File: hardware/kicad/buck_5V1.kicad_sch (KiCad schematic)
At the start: 14 parts, among them J1 12V_IN, J2 12V_IN, Q1 IRF4905

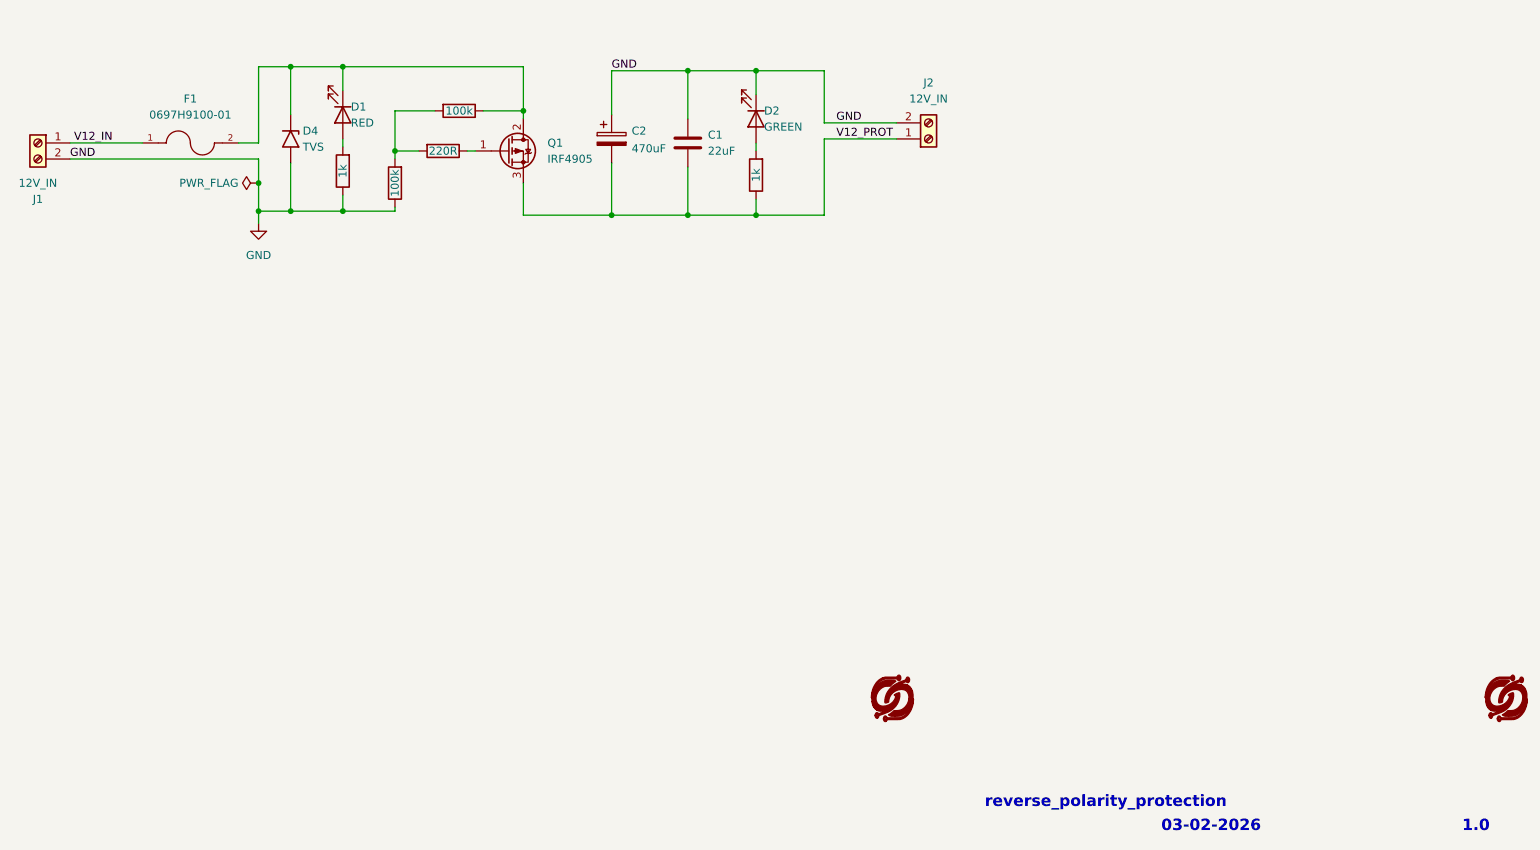
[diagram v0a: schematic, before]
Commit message: feat: added buck_5V1 schematic
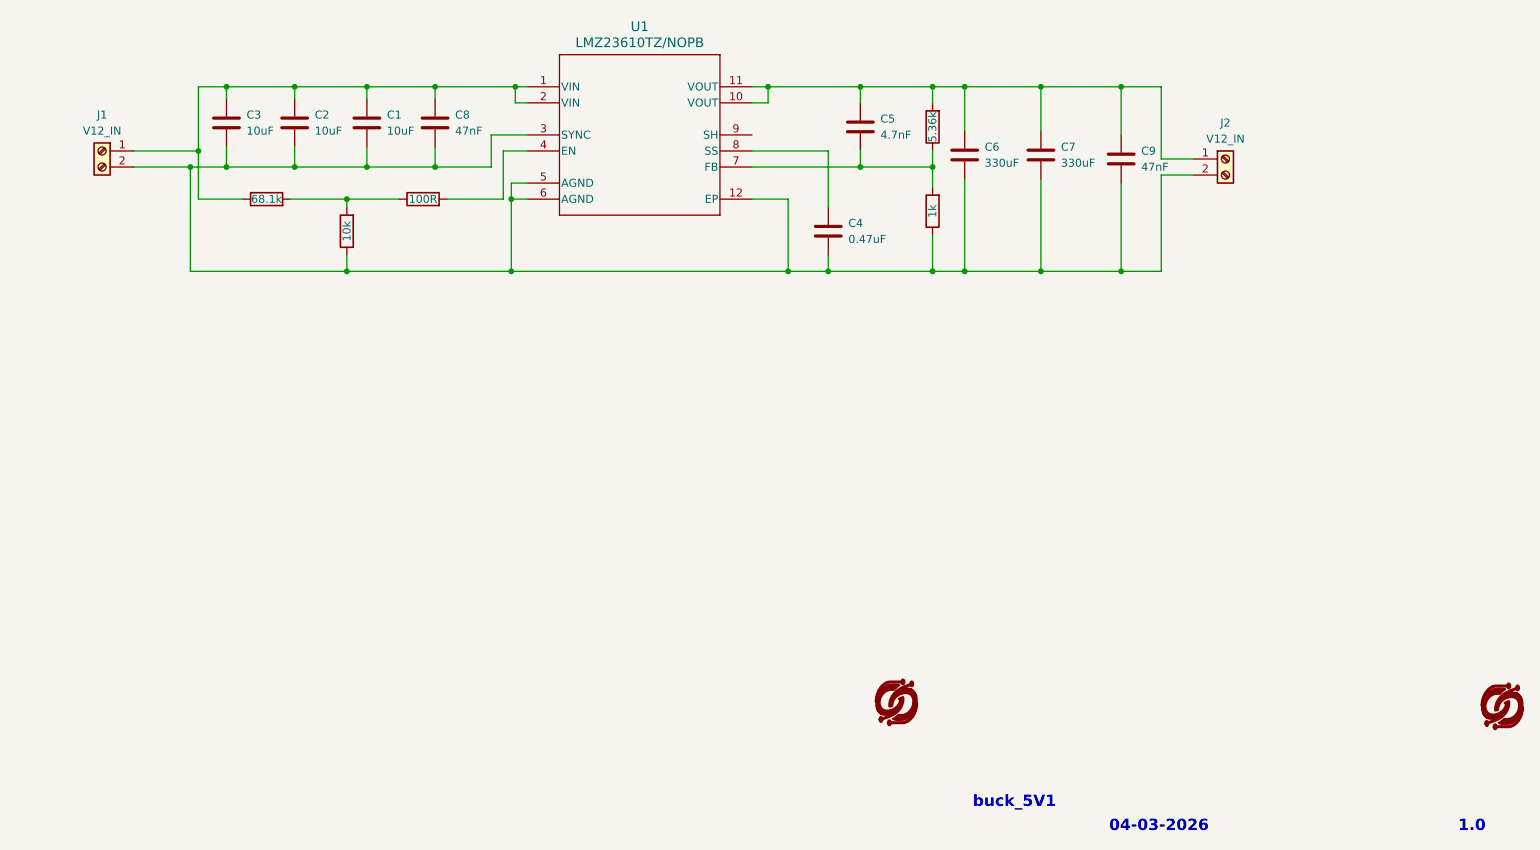
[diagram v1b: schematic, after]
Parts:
- removed C2: 470uF, Capacitor_THT:CP_Radial_D10.0mm_P5.00mm, symbol Device:C_Polarized
- removed D1: RED, LED_THT:LED_D3.0mm, symbol Device:LED
- removed D2: GREEN, LED_THT:LED_D3.0mm, symbol Device:LED
- removed D4: TVS, Diode_THT:D_DO-201AE_P15.24mm_Horizontal, symbol Diode:1.5KExxA
- removed F1: 0697H9100-01, Fuse:FUSRR508W60L835T400H810, symbol Fuse:0697H9100-01
- removed Q1: IRF4905, Package_TO_SOT_THT:TO-220-3_Vertical, symbol Transistor_FET:IRF4905
- added C2, C3: 10uF, symbol Device:C
- added C4: 0.47uF, symbol Device:C
- added C5: 4.7nF, symbol Device:C
- added C6, C7: 330uF, symbol Device:C
- added C8, C9: 47nF, symbol Device:C
- added U1: LMZ23610TZ/NOPB, NDY0011A_N, symbol Buck_5V1:LMZ23610TZ_NOPB
- C1: value 22uF -> 10uF; footprint Capacitor_THT:C_Rect_L7.0mm_W3.5mm_P5.00mm -> (none)
- J1, J2: value 12V_IN -> V12_IN; footprint Terminals:CUI_TB002-500-02BE -> (none)
- R1: value 1k -> 68.1k; footprint Resistor_THT:R_Axial_DIN0207_L6.3mm_D2.5mm_P10.16mm_Horizontal -> (none)
- R2: value 220R -> 10k; footprint Resistor_THT:R_Axial_DIN0207_L6.3mm_D2.5mm_P10.16mm_Horizontal -> (none)
- R3: value 100k -> 100R; footprint Resistor_THT:R_Axial_DIN0207_L6.3mm_D2.5mm_P10.16mm_Horizontal -> (none)
- R4: value 100k -> 5.36k; footprint Resistor_THT:R_Axial_DIN0207_L6.3mm_D2.5mm_P10.16mm_Horizontal -> (none)
- R5: footprint Resistor_THT:R_Axial_DIN0207_L6.3mm_D2.5mm_P10.16mm_Horizontal -> (none)
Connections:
- net at R3.1: now also R1.2, R2.2
- net at R2.1: now also C1.2, J1.2 (Pin_2), J2.2 (Pin_2), R5.1, C2.2, C3.2, C4.2, C6.2, C7.2, C8.2, C9.2, U1.12 (EP), U1.3 (SYNC), U1.5 (AGND), U1.6 (AGND)
- net at R5.2: now also R4.1, C5.2, U1.7 (FB)
- removed net GND: C1.1, J1.2 (Pin_2), J2.2 (Pin_2), R1.1, R4.1
- net V12_IN: no longer names the net of J1.1 (Pin_1)
- net V12_IN: now also C1.1, R1.1, C2.1, C3.1, C8.1, U1.1 (VIN), U1.2 (VIN)
- removed net V12_PROT: C1.2, J2.1 (Pin_1), R5.1
- new net: C5.1, C6.1, C7.1, C9.1, J2.1 (Pin_1), R4.2, U1.10 (VOUT), U1.11 (VOUT)
- new net: R3.2, U1.4 (EN)
- new net: C4.1, U1.8 (SS)
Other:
- note added: "04-03-2026"
- note added: "buck_5V1"
- note removed: "03-02-2026"
- note removed: "reverse_polarity_protection"

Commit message: docs: added export schem for protection circuit
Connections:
- no-connect marks 0 -> 1
